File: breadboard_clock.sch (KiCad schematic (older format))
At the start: 37 parts, among them J1 Conn_01x02_Male, J2 Conn_01x03_Male, P1 R_POT, SW1 SW_Push, SW2 SW_SPDT, SW3 SW_SPDT, U1 ICM7555, U2 74LS04-Full, U3 74LS08-Full, U4 74LS32-Full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

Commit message: Add files via upload
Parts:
- removed SW3: SW_SPDT, Button_Switch_SMD:SW_SPDT_PCM12, symbol Switch:SW_SPDT
- gave numbers to parts that had none: 3
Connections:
- no-connect marks 21 -> 20
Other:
- note added: "Automatic Clock \nClock Speed: X-XX Hz\n"
- note removed: "Automatic Clock \nClock Speed: X-XX Hz, Y Hz when SW3 pressed\n"
- moved on the sheet: C1, C10, C2, C3, C4, C5, C6, C7, C8, C9, D1, D2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

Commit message: Add files via upload
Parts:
- removed U4: 74LS32-Full, Package_SO:SOIC-14_3.9x8.7mm_P1.27mm, symbol Gerig-Added:74LS32-Full
- U2: symbol Gerig-Added:74LS04-Full -> breadboard_clock-rescue:74LS04-Full-Gerig-Added
- U3: symbol Gerig-Added:74LS08-Full -> breadboard_clock-rescue:74LS08-Full-Gerig-Added
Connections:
- net labels removed: HALT
- wire segments 173 -> 183
- no-connect marks 20 -> 7
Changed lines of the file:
@@
 Wire Wire Line
 	4790 2300 4790 2400
-Connection ~ 4790 2650
 Connection ~ 4790 2400
 Wire Wire Line
@@
 Wire Wire Line
 	10640 1500 10840 1500
-Text GLabel 3690 5525 2    50   Input ~ 0
-HALT
 Wire Wire Line
 	8040 4650 8040 4750
@@
 	0    -1   -1   0
 $EndComp
+Text GLabel 9990 4650 1    50   Input ~ 0
+CLK
 Text GLabel 9890 4650 1    50   Input ~ 0
-CLK
-Text GLabel 9990 4650 1    50   Input ~ 0
 ~CLK
 Text GLabel 10090 4650 1    50   Input ~ 0
@@
 	-1   0    0    1
 $EndComp
-$Comp
-L Gerig-Added:74LS32-Full U4
-U 1 1 60435E25
-P 6265 5275
-F 0 "U4" H 6240 5890 50  0000 C CNN
-F 1 "74LS32-Full" H 6240 5799 50  0000 C CNN
-F 2 "Package_SO:SOIC-14_3.9x8.7mm_P1.27mm" H 5415 5775 50  0001 C CNN
-F 3 "" H 5865 5775 50  0001 C CNN
-	1    6265 5275
-	1    0    0    -1
-$EndComp
-$Comp
-L Gerig-Added:74LS04-Full U2
-U 1 1 60437E78
-P 3240 5325
-F 0 "U2" H 3215 5940 50  0000 C CNN
-F 1 "74LS04-Full" H 3215 5849 50  0000 C CNN
-F 2 "Package_SO:SOIC-14_3.9x8.7mm_P1.27mm" H 3190 5725 50  0001 C CNN
-F 3 "" H 3190 5725 50  0001 C CNN
-	1    3240 5325
-	1    0    0    -1
-$EndComp
-$Comp
-L Gerig-Added:74LS08-Full U3
-U 1 1 60439D22
-P 4765 5300
-F 0 "U3" H 4740 5915 50  0000 C CNN
-F 1 "74LS08-Full" H 4740 5824 50  0000 C CNN
-F 2 "Package_SO:SOIC-14_3.9x8.7mm_P1.27mm" H 4665 5800 50  0001 C CNN
-F 3 "" H 4665 5800 50  0001 C CNN
-	1    4765 5300
-	1    0    0    -1
-$EndComp
 Wire Wire Line
 	3915 1500 4265 5000
@@
 Wire Wire Line
 	4140 5300 4265 5300
-Wire Wire Line
-	4265 5500 4165 5500
-Wire Wire Line
-	4165 5500 4165 5875
-Wire Wire Line
-	4165 5875 5615 5875
-Wire Wire Line
-	5615 5875 5615 5075
-Wire Wire Line
-	5615 5075 5765 5075
-Wire Wire Line
-	4265 5200 4165 5200
-Wire Wire Line
-	4165 5200 4165 4525
-Wire Wire Line
-	4165 4525 5615 4525
-Wire Wire Line
-	5615 4525 5615 4975
-Wire Wire Line
-	5615 4975 5765 4975
-Wire Wire Line
-	5215 5600 5215 5800
-Wire Wire Line
-	5215 5800 7140 5800
 Wire Wire Line
 	7140 5800 7140 4350
@@
 	8040 4350 8690 4350
 Wire Wire Line
-	5215 5800 4065 5800
-Wire Wire Line
 	4065 5125 3690 5125
-Connection ~ 5215 5800
 Wire Wire Line
 	4065 5125 4065 5800
@@
 Wire Wire Line
 	4190 5400 4265 5400
-Wire Wire Line
-	5465 5175 5465 5500
-Wire Wire Line
-	5465 5500 5215 5500
-Wire Wire Line
-	5465 5175 5765 5175
-Wire Wire Line
-	3690 5625 3690 5700
-Wire Wire Line
-	3690 5700 5390 5700
-Wire Wire Line
-	5390 5700 5390 5400
-Wire Wire Line
-	5390 5400 5215 5400
-NoConn ~ 2740 5225
-NoConn ~ 2740 5325
-NoConn ~ 2740 5425
-NoConn ~ 2740 5525
-NoConn ~ 3690 5325
-NoConn ~ 3690 5425
-NoConn ~ 5215 5100
-NoConn ~ 5215 5200
-NoConn ~ 5215 5300
-NoConn ~ 5765 5275
-NoConn ~ 5765 5375
-NoConn ~ 5765 5475
-NoConn ~ 6715 5075
-NoConn ~ 6715 5175
-NoConn ~ 6715 5275
-NoConn ~ 6715 5375
-NoConn ~ 6715 5475
-NoConn ~ 6715 5575
 $Comp
 L power:VCC #PWR0101
@@
 $EndComp
 $Comp
-L power:VCC #PWR0102
-U 1 1 60664CD3
-P 5215 5000
-F 0 "#PWR0102" H 5215 4850 50  0001 C CNN
-F 1 "VCC" V 5232 5128 50  0000 L CNN
-F 2 "" H 5215 5000 50  0001 C CNN
-F 3 "" H 5215 5000 50  0001 C CNN
-	1    5215 5000
-	0    1    1    0
-$EndComp
-$Comp
-L power:VCC #PWR0103
-U 1 1 6066BE77
-P 6715 4975
-F 0 "#PWR0103" H 6715 4825 50  0001 C CNN
-F 1 "VCC" V 6732 5103 50  0000 L CNN
-F 2 "" H 6715 4975 50  0001 C CNN
-F 3 "" H 6715 4975 50  0001 C CNN
-	1    6715 4975
-	0    1    1    0
-$EndComp
-$Comp
 L power:GND #PWR0104
 U 1 1 60677C06
@@
 F 3 "" H 2740 5625 50  0001 C CNN
 	1    2740 5625
-	1    0    0    -1
-$EndComp
-$Comp
-L power:GND #PWR0105
-U 1 1 6067AC96
-P 4265 5600
-F 0 "#PWR0105" H 4265 5350 50  0001 C CNN
-F 1 "GND" H 4270 5427 50  0000 C CNN
-F 2 "" H 4265 5600 50  0001 C CNN
-F 3 "" H 4265 5600 50  0001 C CNN
-	1    4265 5600
-	1    0    0    -1
-$EndComp
-$Comp
-L power:GND #PWR0106
-U 1 1 60682119
-P 5765 5575
-F 0 "#PWR0106" H 5765 5325 50  0001 C CNN
-F 1 "GND" H 5770 5402 50  0000 C CNN
-F 2 "" H 5765 5575 50  0001 C CNN
-F 3 "" H 5765 5575 50  0001 C CNN
-	1    5765 5575
 	1    0    0    -1
 $EndComp
@@
 Wire Wire Line
 	4630 1900 4630 2650
-Wire Wire Line
-	4630 2650 4790 2650
 Connection ~ 3650 1500
 Wire Wire Line
@@
 Wire Wire Line
 	4790 2400 5840 2400
-Wire Wire Line
-	4790 2650 4795 2650
 Wire Wire Line
 	5190 1000 5840 1000
@@
 U 1 1 6029DDCC
 P 4210 1705
-F 0 "C9" H 4000 1955 50  0000 L CNN
-F 1 "0.1uF" H 3935 1865 50  0000 L CNN
+F 0 "C9" H 4215 1835 50  0000 L CNN
+F 1 "0.1uF" H 4220 1615 50  0000 L CNN
 F 2 "Capacitor_SMD:C_0805_2012Metric" H 4248 1555 50  0001 C CNN
 F 3 "~" H 4210 1705 50  0001 C CNN
@@
 	1    0    0    -1
 $EndComp
-Connection ~ 2540 2200
+Connection ~ 8540 1950
 Wire Wire Line
 	2540 2200 2590 2200
-Connection ~ 8540 1950
 Wire Wire Line
 	1440 2200 2590 2200
+$Comp
+L breadboard_clock-rescue:74LS04-Full-Gerig-Added U2
+U 1 1 60437E78
+P 3240 5325
+F 0 "U2" H 3215 5940 50  0000 C CNN
+F 1 "74LS04-Full" H 3215 5849 50  0000 C CNN
+F 2 "Package_SO:SOIC-14_3.9x8.7mm_P1.27mm" H 3190 5725 50  0001 C CNN
+F 3 "" H 3190 5725 50  0001 C CNN
+	1    3240 5325
+	1    0    0    -1
+$EndComp
+$Comp
+L power:GND #PWR0105
+U 1 1 6067AC96
+P 4265 5600
+F 0 "#PWR0105" H 4265 5350 50  0001 C CNN
+F 1 "GND" H 4270 5427 50  0000 C CNN
+F 2 "" H 4265 5600 50  0001 C CNN
+F 3 "" H 4265 5600 50  0001 C CNN
+	1    4265 5600
+	1    0    0    -1
+$EndComp
+$Comp
+L breadboard_clock-rescue:74LS08-Full-Gerig-Added U3
+U 1 1 60439D22
+P 4765 5300
+F 0 "U3" H 4740 5915 50  0000 C CNN
+F 1 "74LS08-Full" H 4740 5824 50  0000 C CNN
+F 2 "Package_SO:SOIC-14_3.9x8.7mm_P1.27mm" H 4665 5800 50  0001 C CNN
+F 3 "" H 4665 5800 50  0001 C CNN
+	1    4765 5300
+	1    0    0    -1
+$EndComp
+Wire Wire Line
+	2740 5225 2250 5225
+Wire Wire Line
+	2250 5225 2250 4540
+Wire Wire Line
+	2250 4540 4100 4540
+Wire Wire Line
+	4100 4540 4100 5200
+Wire Wire Line
+	2740 5325 2575 5325
+Wire Wire Line
+	2575 5325 2575 6065
+Wire Wire Line
+	2575 6065 5810 6065
+Wire Wire Line
+	5810 6065 5810 5200
+Wire Wire Line
+	5810 5200 5215 5200
+Wire Wire Line
+	2740 5425 2655 5425
+Wire Wire Line
+	2655 5425 2650 5975
+Wire Wire Line
+	2650 5975 3945 5975
+Wire Wire Line
+	3945 5975 3945 5500
+Wire Wire Line
+	3945 5500 4265 5500
+Wire Wire Line
+	2740 5525 2340 5525
+Wire Wire Line
+	2340 5525 2340 6205
+Wire Wire Line
+	2340 6205 5410 6205
+Wire Wire Line
+	5410 6205 5410 5100
+Wire Wire Line
+	5410 5100 5215 5100
+NoConn ~ 3690 5525
+NoConn ~ 3690 5625
+$Comp
+L power:VCC #PWR?
+U 1 1 60C9BE17
+P 5215 5000
+F 0 "#PWR?" H 5215 4850 50  0001 C CNN
+F 1 "VCC" V 5232 5128 50  0000 L CNN
+F 2 "" H 5215 5000 50  0001 C CNN
+F 3 "" H 5215 5000 50  0001 C CNN
+	1    5215 5000
+	0    1    1    0
+$EndComp
+Wire Wire Line
+	4100 5200 4265 5200
+Wire Wire Line
+	3690 5325 4030 5325
+Wire Wire Line
+	4030 5325 4030 5995
+Wire Wire Line
+	4030 5995 5375 5995
+Wire Wire Line
+	5375 5995 5375 5300
+Wire Wire Line
+	5375 5300 5215 5300
+Wire Wire Line
+	3815 5425 3815 6135
+Wire Wire Line
+	3815 6135 5320 6135
+Wire Wire Line
+	3690 5425 3815 5425
+Wire Wire Line
+	5320 6135 5320 5800
+Connection ~ 5320 5800
+Wire Wire Line
+	5320 5800 7140 5800
+Wire Wire Line
+	4065 5800 5320 5800
+Wire Wire Line
+	4630 2650 4790 2650
+Connection ~ 4790 2650
+NoConn ~ 5215 5400
+NoConn ~ 5215 5500
+NoConn ~ 5215 5600
 $EndSCHEMATC

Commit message: Add files via upload
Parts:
- added D6, D7, D8, D9: D_Schottky, Diode_SMD:D_0805_2012Metric_Pad1.15x1.40mm_HandSolder, symbol Device:D_Schottky
- added J3: USB_C_Receptacle_USB2.0, Connector_USB:USB_C_Receptacle_Amphenol_12401610E4-2A, symbol Connector:USB_C_Receptacle_USB2.0
- C7: value 0.1uF -> 1uF
- D5: footprint (none) -> Diode_SMD:D_0805_2012Metric_Pad1.15x1.40mm_HandSolder
- P1: value R_POT -> 1M; footprint Gerig-Added:Potentiomter_Bourns_PDB12_THT -> Potentiometer_SMD:Potentiometer_Bourns_3224X_Vertical
- U5, U8: footprint Package_SO:SOIC-8-1EP_3.9x4.9mm_P1.27mm_EP2.29x3mm -> Package_SO:SOIC-8-N7_3.9x4.9mm_P1.27mm
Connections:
- net labels added: PowerSupply+, PowerSupply-
- wire segments 183 -> 205
- no-connect marks 7 -> 12
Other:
- note added: "Automatic Clock \nClock Speed: .5-7 Hz\n"
- note removed: "Automatic Clock \nClock Speed: X-XX Hz\n"
- moved on the sheet: C6, C7, J1, J2, U3

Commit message: Add files via upload
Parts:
- added D10: LED, LED_SMD:LED_0805_2012Metric, symbol Device:LED
- added R11: 220, Resistor_SMD:R_0805_2012Metric, symbol Device:R
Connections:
- net GND: now also R11.2
- net ~CLK: now also D10.2 (A)
- new net: D10.1 (K), R11.1
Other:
- moved on the sheet: C1, C10, C2, C3, C4, C5, C6, C7, C8, C9, D1, D2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

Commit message: Add files via upload
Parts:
- P1: footprint Potentiometer_SMD:Potentiometer_Bourns_3224X_Vertical -> Potentiometer_SMD:Potentiometer_Bourns_3214J_Horizontal
- SW1: footprint Button_Switch_SMD:SW_SPST_B3S-1000 -> Button_Switch_SMD:SW_SPST_B3U-1100P-B
- U1: footprint Package_SO:SOIC-8-1EP_3.9x4.9mm_P1.27mm_EP2.29x3mm -> Package_SO:SOIC-8_3.9x4.9mm_P1.27mm
- U5, U8: footprint Package_SO:SOIC-8-N7_3.9x4.9mm_P1.27mm -> Package_SO:SOIC-8_3.9x4.9mm_P1.27mm
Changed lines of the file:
@@
 F 0 "U1" H 6440 3800 50  0000 C CNN
 F 1 "ICM7555" H 6340 4500 50  0000 C CNN
-F 2 "Package_SO:SOIC-8-1EP_3.9x4.9mm_P1.27mm_EP2.29x3mm" H 6140 4150 50  0001 C CNN
+F 2 "Package_SO:SOIC-8_3.9x4.9mm_P1.27mm" H 6140 4150 50  0001 C CNN
 F 3 "http://www.intersil.com/content/dam/Intersil/documents/icm7/icm7555-56.pdf" H 6140 4150 50  0001 C CNN
 	1    6140 4150
@@
 F 0 "P1" H 7270 4104 50  0000 R CNN
 F 1 "1M" H 7270 4195 50  0000 R CNN
-F 2 "Potentiometer_SMD:Potentiometer_Bourns_3224X_Vertical" H 7340 4150 50  0001 C CNN
+F 2 "Potentiometer_SMD:Potentiometer_Bourns_3214J_Horizontal" H 7340 4150 50  0001 C CNN
 F 3 "~" H 7340 4150 50  0001 C CNN
 	1    7340 4150
@@
 F 0 "U5" H 10190 3800 50  0000 C CNN
 F 1 "ICM7555" H 10090 4500 50  0000 C CNN
-F 2 "Package_SO:SOIC-8-N7_3.9x4.9mm_P1.27mm" H 9890 4150 50  0001 C CNN
+F 2 "Package_SO:SOIC-8_3.9x4.9mm_P1.27mm" H 9890 4150 50  0001 C CNN
 F 3 "http://www.intersil.com/content/dam/Intersil/documents/icm7/icm7555-56.pdf" H 9890 4150 50  0001 C CNN
 	1    9890 4150
@@
 F 0 "SW1" V 8910 4330 50  0000 C CNN
 F 1 "SW_Push" V 9000 4320 50  0000 C CNN
-F 2 "Button_Switch_SMD:SW_SPST_B3S-1000" H 8680 4350 50  0001 C CNN
+F 2 "Button_Switch_SMD:SW_SPST_B3U-1100P-B" H 8680 4350 50  0001 C CNN
 F 3 "~" H 8680 4350 50  0001 C CNN
 	1    8680 4150
@@
 F 0 "U8" H 13390 3850 50  0000 C CNN
 F 1 "ICM7555" H 13290 4550 50  0000 C CNN
-F 2 "Package_SO:SOIC-8-N7_3.9x4.9mm_P1.27mm" H 13090 4200 50  0001 C CNN
+F 2 "Package_SO:SOIC-8_3.9x4.9mm_P1.27mm" H 13090 4200 50  0001 C CNN
 F 3 "http://www.intersil.com/content/dam/Intersil/documents/icm7/icm7555-56.pdf" H 13090 4200 50  0001 C CNN
 	1    13090 4200

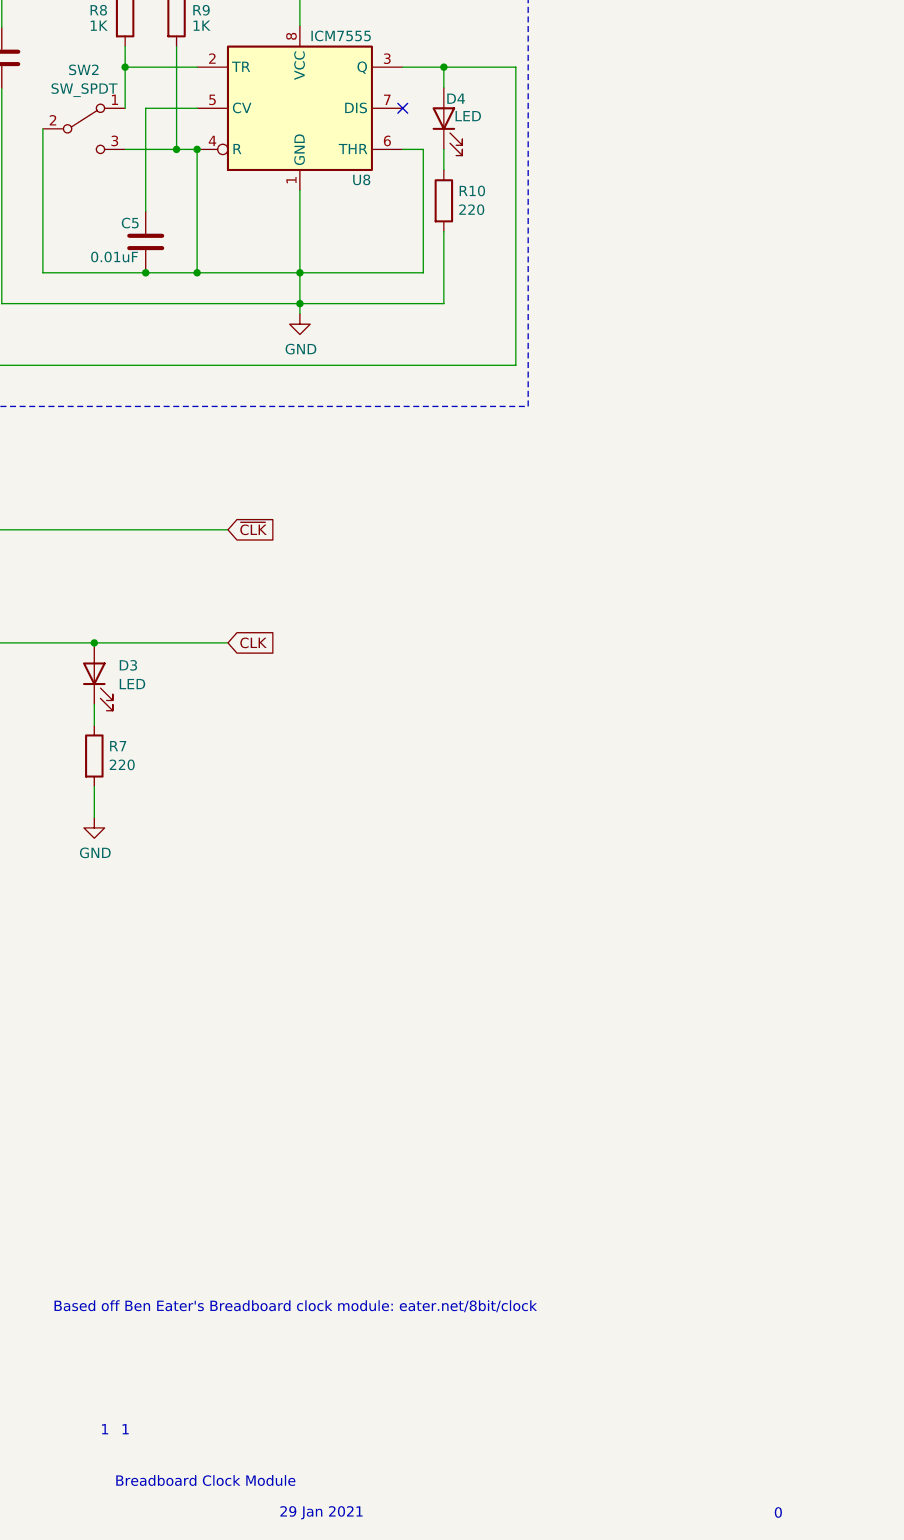
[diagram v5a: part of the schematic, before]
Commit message: Add files via upload
Modified PCB/Schematic to get clock switching 555 circuit working. Trace was leading from pin 4 to GND, causing this 555 to always be in "reset" mode.
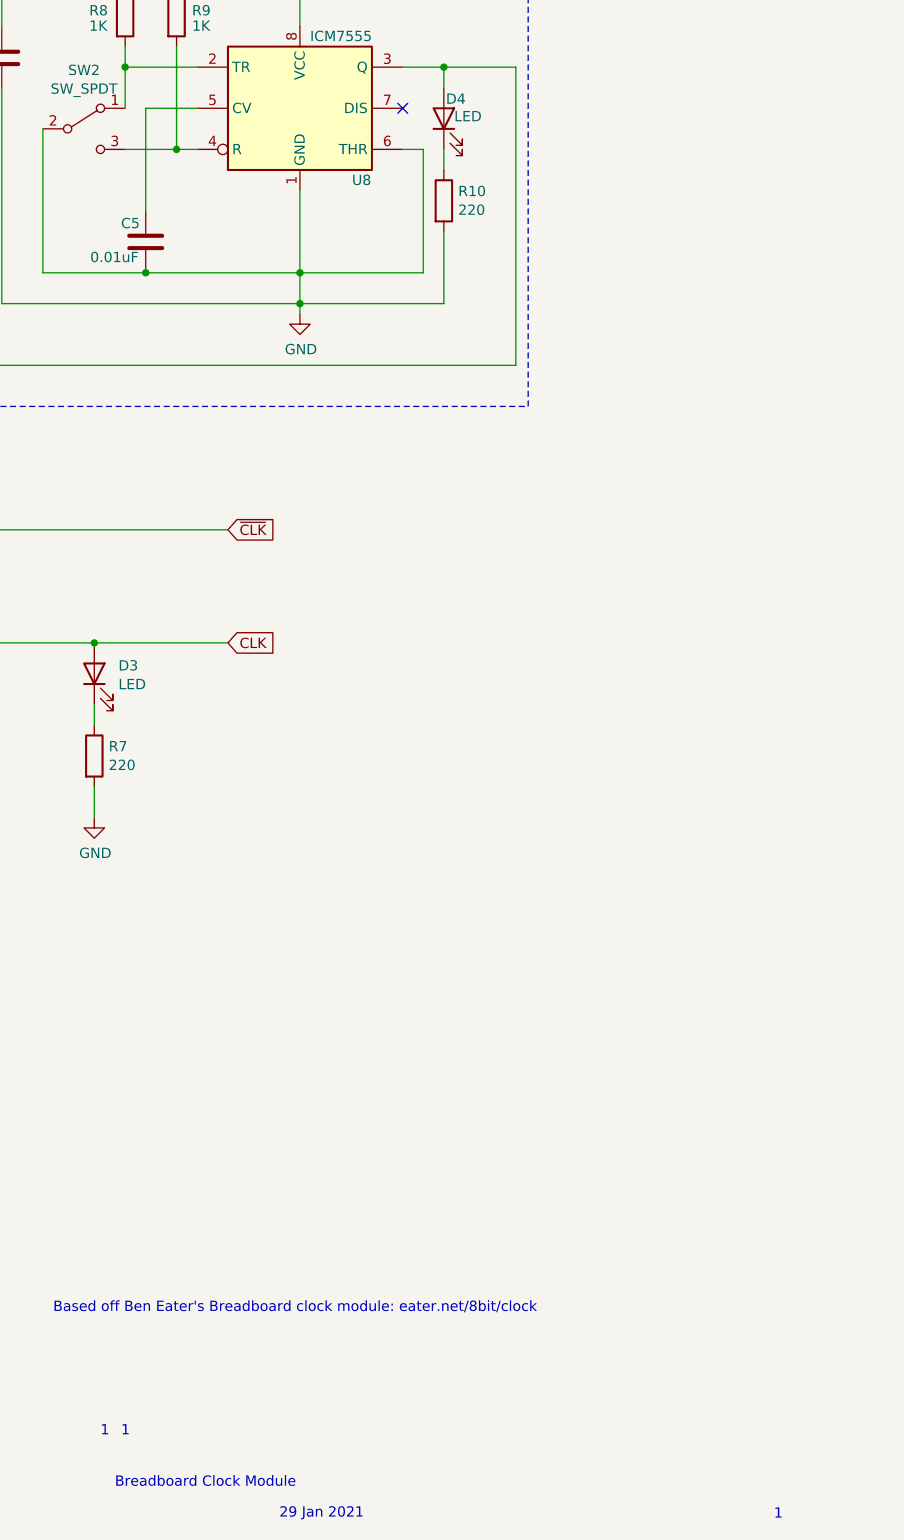
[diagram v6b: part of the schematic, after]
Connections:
- net GND: no longer R9.2, SW2.3 (C), U8.4 (R)
- new net: R9.2, SW2.3 (C), U8.4 (R)
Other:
- note removed: "0"
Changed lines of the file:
@@
 Text Notes 12220 10665 0    50   ~ 0
 1
-Text Notes 15395 11070 0    50   ~ 0
-0
 $Comp
 L power:GND #PWR09
@@
 Wire Wire Line
 	6140 4550 6140 5200
-Wire Wire Line
-	12340 5000 12590 5000
-Connection ~ 12590 5000
-Wire Wire Line
-	12590 5000 13090 5000
-Wire Wire Line
-	12590 4400 12590 5000
 $Comp
 L Device:C C8
@@
 	1    0    0    -1
 $EndComp
-Connection ~ 12590 4400
 Wire Wire Line
 	5490 4650 6640 4650
@@
 Wire Notes Line
 	14200 2950 11400 2950
+Wire Wire Line
+	12340 5000 13090 5000
+Text Notes 15395 11070 0    50   ~ 0
+1
 $EndSCHEMATC
